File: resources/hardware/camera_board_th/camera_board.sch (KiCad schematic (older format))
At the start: 10 parts, among them P1 CONN_01X02

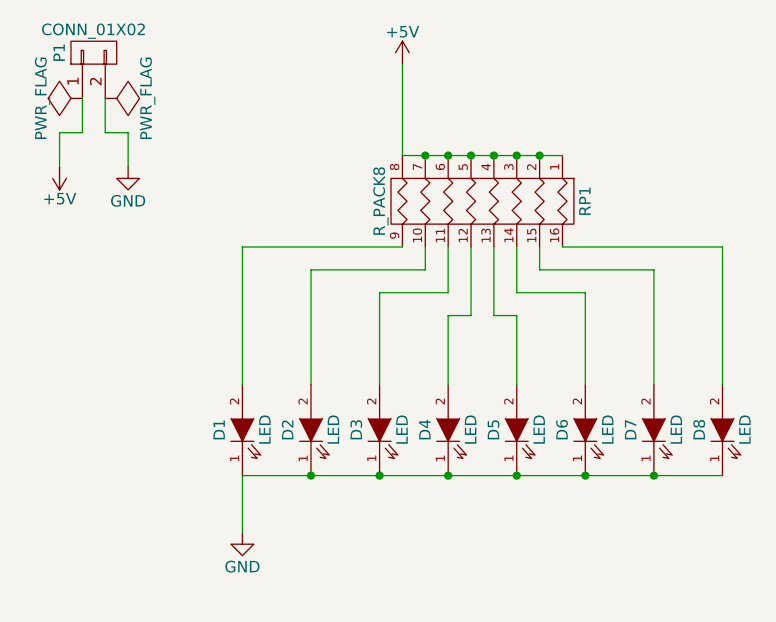
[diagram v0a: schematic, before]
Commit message: new version of headband sketch, reworked camera board on 4 led version
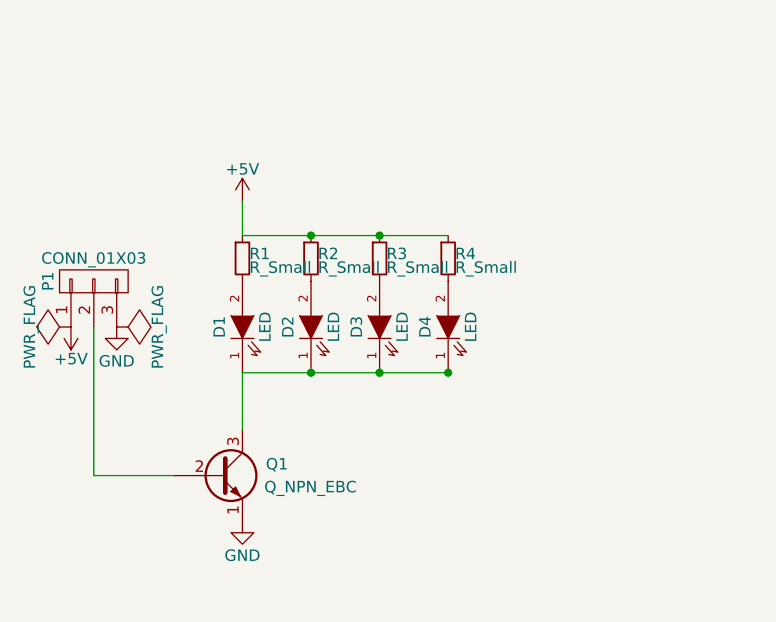
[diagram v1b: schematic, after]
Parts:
- removed D5, D6, D7, D8: LED, LEDs:LED-3MM, symbol LED
- removed P1: CONN_01X02, Pin_Headers:Pin_Header_Angled_1x02, symbol CONN_01X02
- removed RP1: R_PACK8, Housings_DIP:DIP-16_W7.62mm, symbol R_PACK8
- added P1: CONN_01X03, symbol CONN_01X03
- added Q1: Q_NPN_EBC, symbol Q_NPN_EBC
- added R1, R2, R3, R4: R_Small, symbol R_Small
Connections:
- net +5V: now also P1.1 (P1), R1.1, R2.1, R3.1, R4.1
- net GND: now also P1.3 (P3), Q1.1 (E); no longer D1.1 (K), D2.1 (K), D3.1 (K), D4.1 (K)
- net at D1.2 (A): now also R1.2
- net at D2.2 (A): now also R2.2
- net at D3.2 (A): now also R3.2
- net at D4.2 (A): now also R4.2
- new net: D1.1 (K), D2.1 (K), D3.1 (K), D4.1 (K), Q1.3 (C)
- new net: P1.2 (P2), Q1.2 (B)
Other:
- moved on the sheet: D1, D2, D3, D4

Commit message: nt
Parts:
- added R5: R_Small, symbol R_Small
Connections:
- net at Q1.2 (B): now also R5.1; no longer P1.2 (P2)
- new net SGNL: P1.2 (P2), R5.2
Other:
- moved on the sheet: Q1
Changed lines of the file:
@@
 L GND #PWR02
 U 1 1 569CFB31
-P 3750 4250
-F 0 "#PWR02" H 3750 4000 50  0001 C CNN
-F 1 "GND" H 3750 4100 50  0000 C CNN
-F 2 "" H 3750 4250 50  0000 C CNN
-F 3 "" H 3750 4250 50  0000 C CNN
-	1    3750 4250
+P 3750 4400
+F 0 "#PWR02" H 3750 4150 50  0001 C CNN
+F 1 "GND" H 3750 4250 50  0000 C CNN
+F 2 "" H 3750 4400 50  0000 C CNN
+F 3 "" H 3750 4400 50  0000 C CNN
+	1    3750 4400
 	1    0    0    -1
 $EndComp
@@
 L Q_NPN_EBC Q1
 U 1 1 56E033A4
-P 3650 4050
-F 0 "Q1" H 3950 4100 50  0000 R CNN
-F 1 "Q_NPN_EBC" H 4250 4000 50  0000 R CNN
-F 2 "" H 3850 4150 50  0000 C CNN
-F 3 "" H 3650 4050 50  0000 C CNN
-	1    3650 4050
+P 3650 4200
+F 0 "Q1" H 3950 4250 50  0000 R CNN
+F 1 "Q_NPN_EBC" H 4250 4150 50  0000 R CNN
+F 2 "" H 3850 4300 50  0000 C CNN
+F 3 "" H 3650 4200 50  0000 C CNN
+	1    3650 4200
 	1    0    0    -1
 $EndComp
@@
 	-1   0    0    1
 $EndComp
-Connection ~ 4050 3600
-Connection ~ 4350 3600
-Wire Wire Line
-	3750 3600 4650 3600
-Connection ~ 4650 3600
-Wire Wire Line
-	3100 3400 3100 4050
-Wire Wire Line
-	3100 4050 3450 4050
 $Comp
 L R_Small R1
@@
 	1    0    0    -1
 $EndComp
+Connection ~ 4050 3600
+Connection ~ 4350 3600
+Wire Wire Line
+	3750 3600 4650 3600
+Connection ~ 4650 3600
 Wire Wire Line
 	3750 3000 4650 3000
@@
 Wire Wire Line
 	3750 2850 3750 3000
+Text Label 3100 3800 0    60   ~ 0
+SGNL
+$Comp
+L R_Small R5
+U 1 1 56E03C9D
+P 3350 4200
+F 0 "R5" H 3380 4220 50  0000 L CNN
+F 1 "R_Small" H 3380 4160 50  0000 L CNN
+F 2 "" H 3350 4200 50  0000 C CNN
+F 3 "" H 3350 4200 50  0000 C CNN
+	1    3350 4200
+	0    1    1    0
+$EndComp
 Wire Wire Line
-	3750 3850 3750 3600
+	3100 3400 3100 4200
+Wire Wire Line
+	3100 4200 3250 4200
+Wire Wire Line
+	3750 4000 3750 3600
 $EndSCHEMATC
